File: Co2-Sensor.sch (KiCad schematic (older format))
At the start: 75 parts, among them J1 OLED, J2 SCD30, J3 LED, J4 Power, J5 USB_C_Receptacle_USB2.0, J6 LED, J7 SPS30, J8 I2C, Q1 S8050, Q2 S8050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

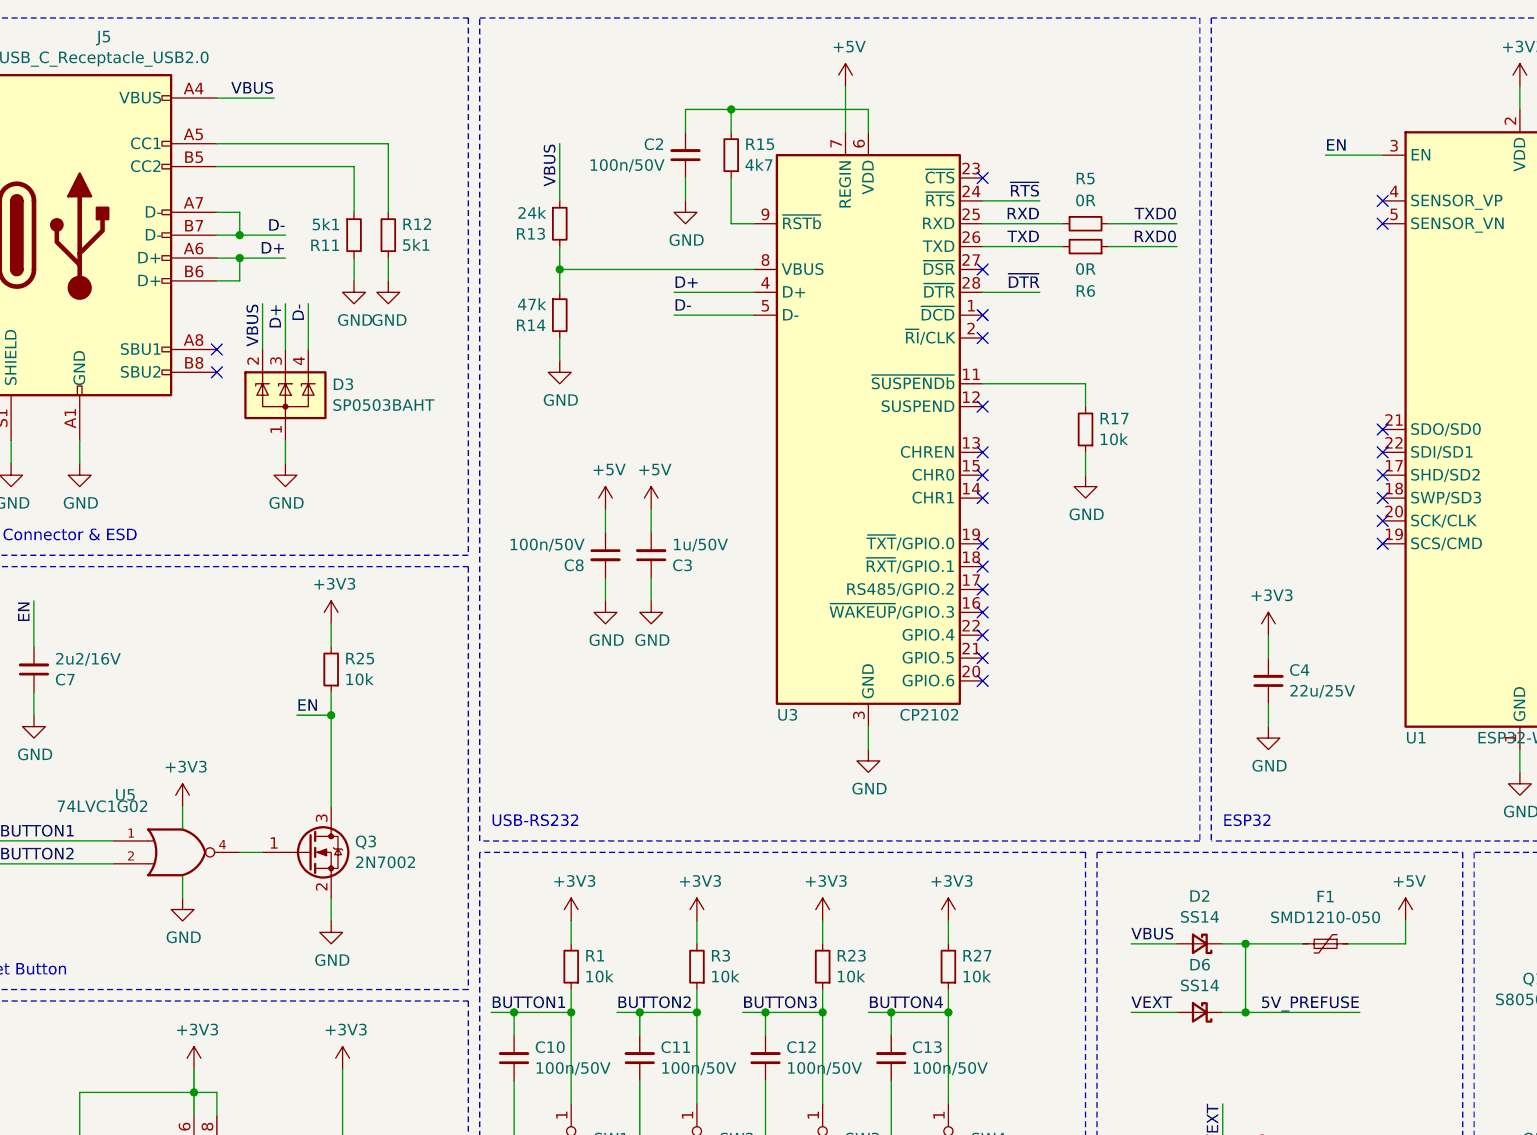
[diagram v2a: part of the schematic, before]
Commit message: Add more capacitance to ESP
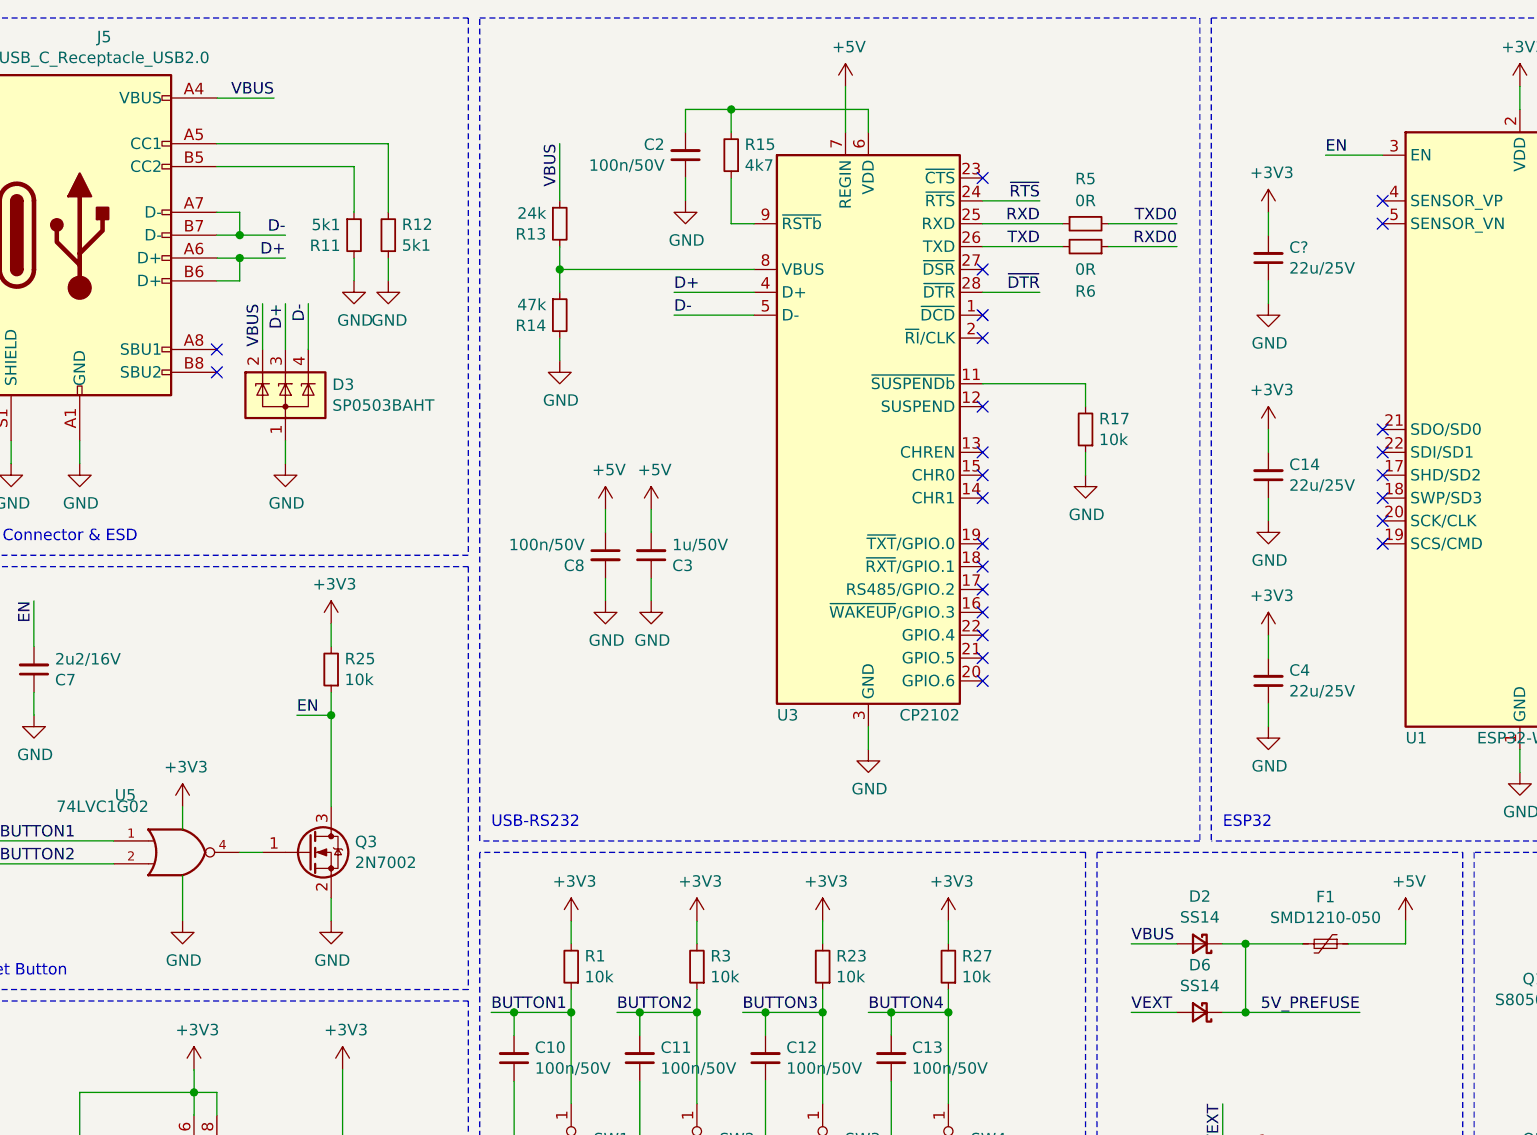
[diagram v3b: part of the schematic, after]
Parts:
- added C14, C?: 22u/25V, Capacitor_SMD:C_0805_2012Metric, symbol Device:C_Small
- C10, C11, C12, C13, C2, C8, C9: LCSC C24452 -> C14663
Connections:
- net +3V3: now also C14.2, C?.2
- net GND: now also C14.1, C?.1
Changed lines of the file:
@@
 F 2 "Capacitor_SMD:C_0603_1608Metric" H 3750 1150 50  0001 C CNN
 F 3 "~" H 3750 1150 50  0001 C CNN
-F 4 "C24452" H 3750 1150 50  0001 C CNN "LCSC"
+F 4 "C14663" H 3750 1150 50  0001 C CNN "LCSC"
 	1    3750 1150
 	1    0    0    1
@@
 F 2 "Capacitor_SMD:C_0603_1608Metric" H 3400 2900 50  0001 C CNN
 F 3 "~" H 3400 2900 50  0001 C CNN
-F 4 "C24452" H 3400 2900 50  0001 C CNN "LCSC"
+F 4 "C14663" H 3400 2900 50  0001 C CNN "LCSC"
 	1    3400 2900
 	1    0    0    -1
@@
 L power:GND #PWR0158
 U 1 1 5FC7C9D2
-P 1550 4400
-F 0 "#PWR0158" H 1550 4150 50  0001 C CNN
-F 1 "GND" H 1555 4227 50  0000 C CNN
-F 2 "" H 1550 4400 50  0001 C CNN
-F 3 "" H 1550 4400 50  0001 C CNN
-	1    1550 4400
-	1    0    0    -1
-$EndComp
-Wire Wire Line
-	1550 4400 1550 4300
+P 1550 4500
+F 0 "#PWR0158" H 1550 4250 50  0001 C CNN
+F 1 "GND" H 1555 4327 50  0000 C CNN
+F 2 "" H 1550 4500 50  0001 C CNN
+F 3 "" H 1550 4500 50  0001 C CNN
+	1    1550 4500
+	1    0    0    -1
+$EndComp
+Wire Wire Line
+	1550 4500 1550 4300
 $Comp
 L power:+3V3 #PWR0159
@@
 F 2 "Capacitor_SMD:C_0603_1608Metric" H 2250 5700 50  0001 C CNN
 F 3 "~" H 2250 5700 50  0001 C CNN
-F 4 "C24452" H 2250 5700 50  0001 C CNN "LCSC"
+F 4 "C14663" H 2250 5700 50  0001 C CNN "LCSC"
 	1    2250 5700
 	-1   0    0    1
@@
 F 2 "Capacitor_SMD:C_0603_1608Metric" H 3000 5100 50  0001 C CNN
 F 3 "~" H 3000 5100 50  0001 C CNN
-F 4 "C24452" H 3000 5100 50  0001 C CNN "LCSC"
+F 4 "C14663" H 3000 5100 50  0001 C CNN "LCSC"
 	1    3000 5100
 	-1   0    0    1
@@
 F 2 "Capacitor_SMD:C_0603_1608Metric" H 3550 5100 50  0001 C CNN
 F 3 "~" H 3550 5100 50  0001 C CNN
-F 4 "C24452" H 3550 5100 50  0001 C CNN "LCSC"
+F 4 "C14663" H 3550 5100 50  0001 C CNN "LCSC"
 	1    3550 5100
 	-1   0    0    1
@@
 F 2 "Capacitor_SMD:C_0603_1608Metric" H 4100 5100 50  0001 C CNN
 F 3 "~" H 4100 5100 50  0001 C CNN
-F 4 "C24452" H 4100 5100 50  0001 C CNN "LCSC"
+F 4 "C14663" H 4100 5100 50  0001 C CNN "LCSC"
 	1    4100 5100
 	-1   0    0    1
@@
 F 2 "Capacitor_SMD:C_0603_1608Metric" H 4650 5100 50  0001 C CNN
 F 3 "~" H 4650 5100 50  0001 C CNN
-F 4 "C24452" H 4650 5100 50  0001 C CNN "LCSC"
+F 4 "C14663" H 4650 5100 50  0001 C CNN "LCSC"
 	1    4650 5100
 	-1   0    0    1
@@
 Wire Wire Line
 	2200 3600 2200 4000
+$Comp
+L power:+3V3 #PWR0167
+U 1 1 5F7B3818
+P 6300 2350
+F 0 "#PWR0167" H 6300 2200 50  0001 C CNN
+F 1 "+3V3" H 6315 2523 50  0000 C CNN
+F 2 "" H 6300 2350 50  0001 C CNN
+F 3 "" H 6300 2350 50  0001 C CNN
+	1    6300 2350
+	1    0    0    -1
+$EndComp
+Wire Wire Line
+	6300 2350 6300 2450
+$Comp
+L power:GND #PWR0168
+U 1 1 5F7B381F
+P 6300 2750
+F 0 "#PWR0168" H 6300 2500 50  0001 C CNN
+F 1 "GND" H 6305 2577 50  0000 C CNN
+F 2 "" H 6300 2750 50  0001 C CNN
+F 3 "" H 6300 2750 50  0001 C CNN
+	1    6300 2750
+	1    0    0    -1
+$EndComp
+Wire Wire Line
+	6300 2750 6300 2650
+$Comp
+L Device:C_Small C14
+U 1 1 5F7B3827
+P 6300 2550
+F 0 "C14" H 6209 2504 50  0000 R CNN
+F 1 "22u/25V" H 6209 2595 50  0000 R CNN
+F 2 "Capacitor_SMD:C_0805_2012Metric" H 6300 2550 50  0001 C CNN
+F 3 "~" H 6300 2550 50  0001 C CNN
+F 4 "C45783" H 6300 2550 50  0001 C CNN "LCSC"
+	1    6300 2550
+	-1   0    0    1
+$EndComp
+$Comp
+L power:+3V3 #PWR?
+U 1 1 5F7CF738
+P 6300 1400
+F 0 "#PWR?" H 6300 1250 50  0001 C CNN
+F 1 "+3V3" H 6315 1573 50  0000 C CNN
+F 2 "" H 6300 1400 50  0001 C CNN
+F 3 "" H 6300 1400 50  0001 C CNN
+	1    6300 1400
+	1    0    0    -1
+$EndComp
+Wire Wire Line
+	6300 1400 6300 1500
+$Comp
+L power:GND #PWR?
+U 1 1 5F7CF73F
+P 6300 1800
+F 0 "#PWR?" H 6300 1550 50  0001 C CNN
+F 1 "GND" H 6305 1627 50  0000 C CNN
+F 2 "" H 6300 1800 50  0001 C CNN
+F 3 "" H 6300 1800 50  0001 C CNN
+	1    6300 1800
+	1    0    0    -1
+$EndComp
+Wire Wire Line
+	6300 1800 6300 1700
+$Comp
+L Device:C_Small C?
+U 1 1 5F7CF747
+P 6300 1600
+F 0 "C?" H 6209 1554 50  0000 R CNN
+F 1 "22u/25V" H 6209 1645 50  0000 R CNN
+F 2 "Capacitor_SMD:C_0805_2012Metric" H 6300 1600 50  0001 C CNN
+F 3 "~" H 6300 1600 50  0001 C CNN
+F 4 "C45783" H 6300 1600 50  0001 C CNN "LCSC"
+	1    6300 1600
+	-1   0    0    1
+$EndComp
 $EndSCHEMATC

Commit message: Revision 2
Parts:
- gave numbers to parts that had none: 1
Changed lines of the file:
@@
 $EndComp
 $Comp
-L power:+3V3 #PWR?
+L power:+3V3 #PWR0169
 U 1 1 5F7CF738
 P 6300 1400
-F 0 "#PWR?" H 6300 1250 50  0001 C CNN
+F 0 "#PWR0169" H 6300 1250 50  0001 C CNN
 F 1 "+3V3" H 6315 1573 50  0000 C CNN
 F 2 "" H 6300 1400 50  0001 C CNN
@@
 	6300 1400 6300 1500
 $Comp
-L power:GND #PWR?
+L power:GND #PWR0170
 U 1 1 5F7CF73F
 P 6300 1800
-F 0 "#PWR?" H 6300 1550 50  0001 C CNN
+F 0 "#PWR0170" H 6300 1550 50  0001 C CNN
 F 1 "GND" H 6305 1627 50  0000 C CNN
 F 2 "" H 6300 1800 50  0001 C CNN
@@
 	6300 1800 6300 1700
 $Comp
-L Device:C_Small C?
+L Device:C_Small C15
 U 1 1 5F7CF747
 P 6300 1600
-F 0 "C?" H 6209 1554 50  0000 R CNN
+F 0 "C15" H 6209 1554 50  0000 R CNN
 F 1 "22u/25V" H 6209 1645 50  0000 R CNN
 F 2 "Capacitor_SMD:C_0805_2012Metric" H 6300 1600 50  0001 C CNN
